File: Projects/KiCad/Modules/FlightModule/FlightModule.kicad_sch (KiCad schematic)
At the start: 66 parts, among them J1 Conn_01x08, J2 Conn_01x02_Pin, J3 Conn_01x02_Pin, J4 Conn_01x02_Pin, J5 Conn_01x02_Pin, J6 Conn_01x02_Pin, Q1 Q_NPN_BEC, Q2 Q_NPN_BEC, SW1 SW_DIP_x02, U1 MCP2562-E-P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

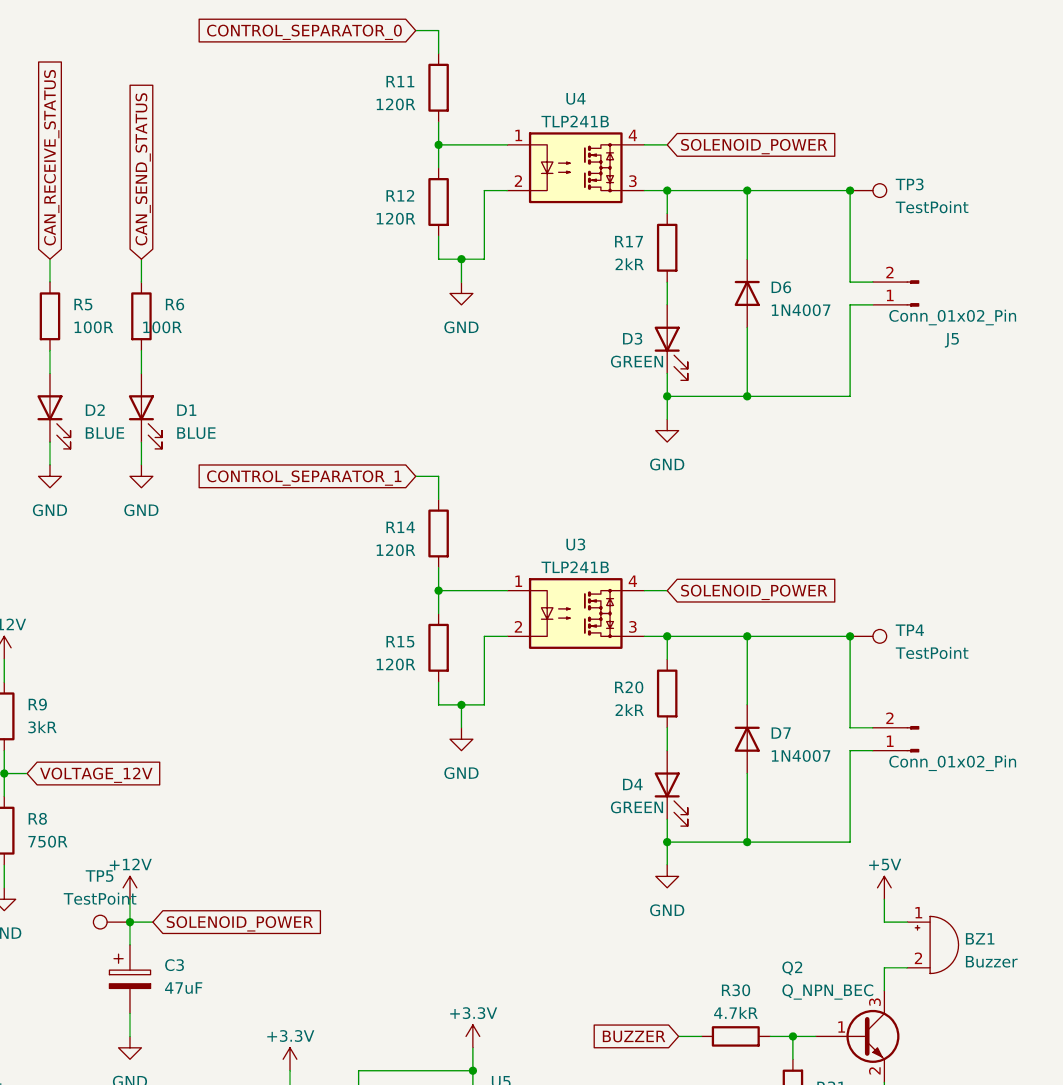
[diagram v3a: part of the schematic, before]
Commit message: 分離制御回路を修正
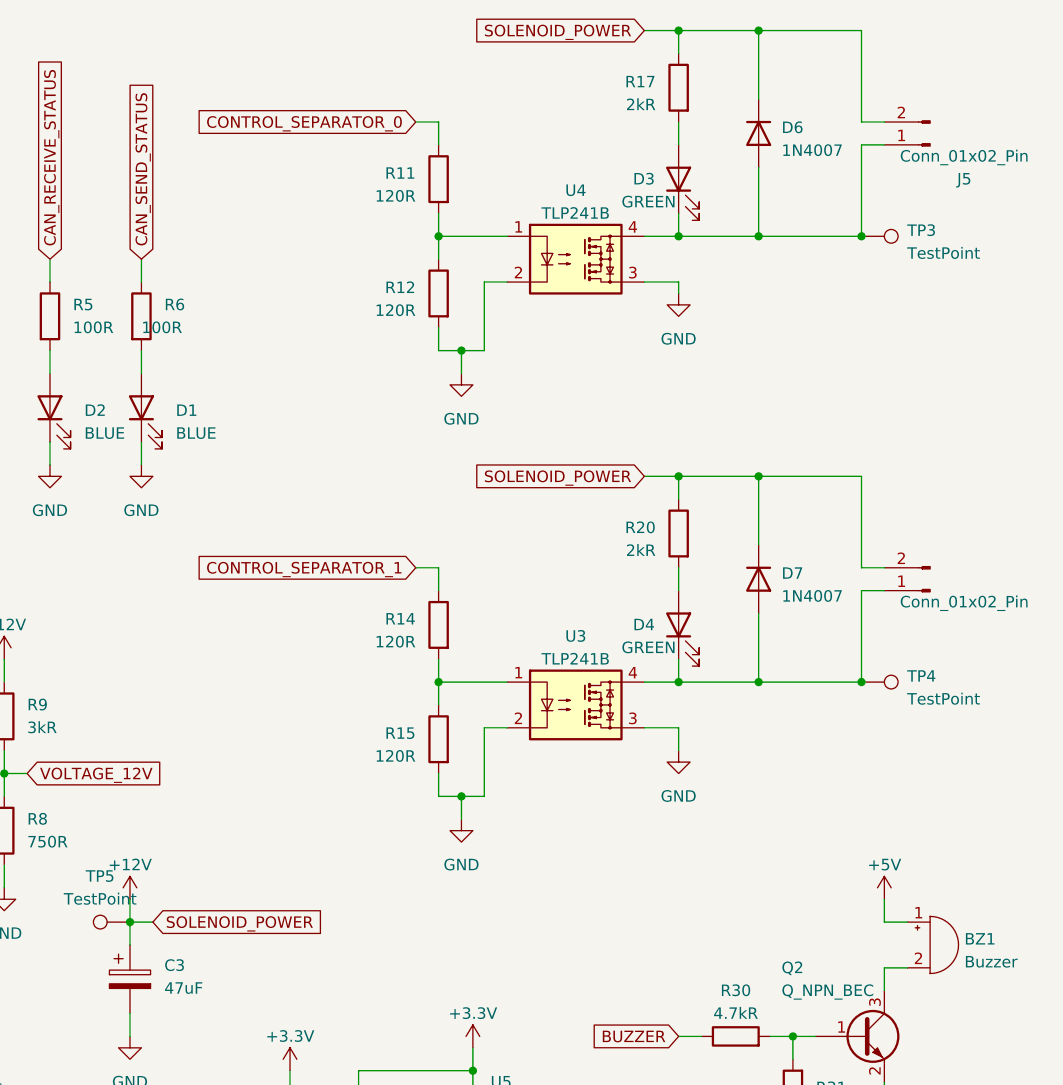
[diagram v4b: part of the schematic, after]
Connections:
- net +12V: now also D6.1 (K), D7.1 (K), J4.2 (Pin_2), J5.2 (Pin_2), R17.1, R20.1; no longer U3.4, U4.4
- net GND: now also U3.3, U4.3; no longer D3.1 (K), D4.1 (K), D6.2 (A), D7.2 (A), J4.1 (Pin_1), J5.1 (Pin_1)
- new net: D3.1 (K), D6.2 (A), J5.1 (Pin_1), TP3.1, U4.4
- new net: D4.1 (K), D7.2 (A), J4.1 (Pin_1), TP4.1, U3.4
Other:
- moved on the sheet: D3, D4, D6, D7, J5, R11, R12, R14, R15, R17, R20, TP3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
